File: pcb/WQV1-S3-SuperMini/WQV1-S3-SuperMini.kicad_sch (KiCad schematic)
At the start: 10 parts, among them U1 ESP32-S3 Super Micro, U2 SSD1306_OLED_128x64, U3 TFDU4101-TR3

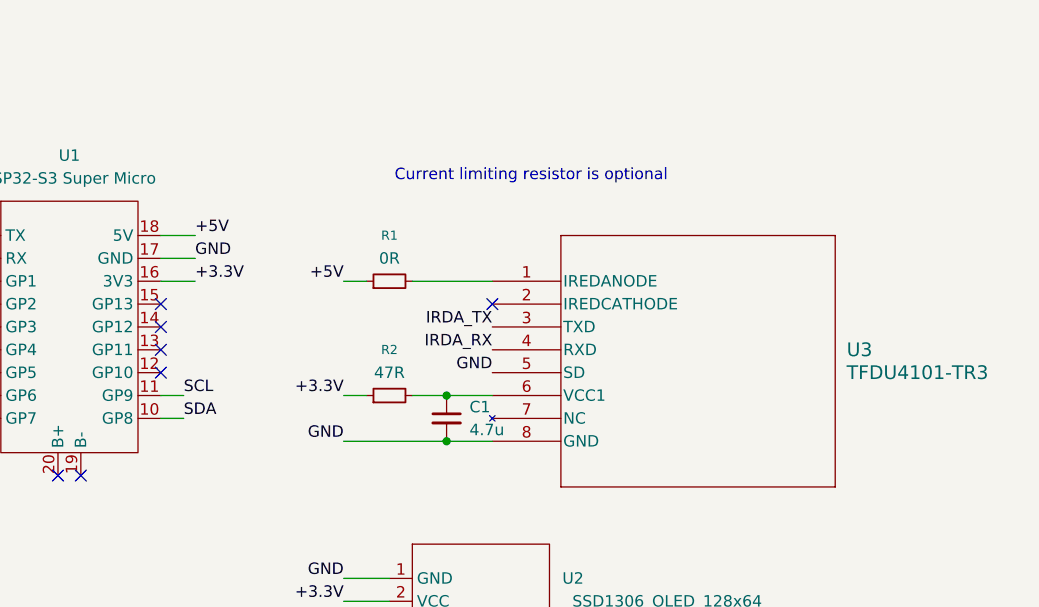
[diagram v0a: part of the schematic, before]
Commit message: PCB revision fixing through-hole spacing
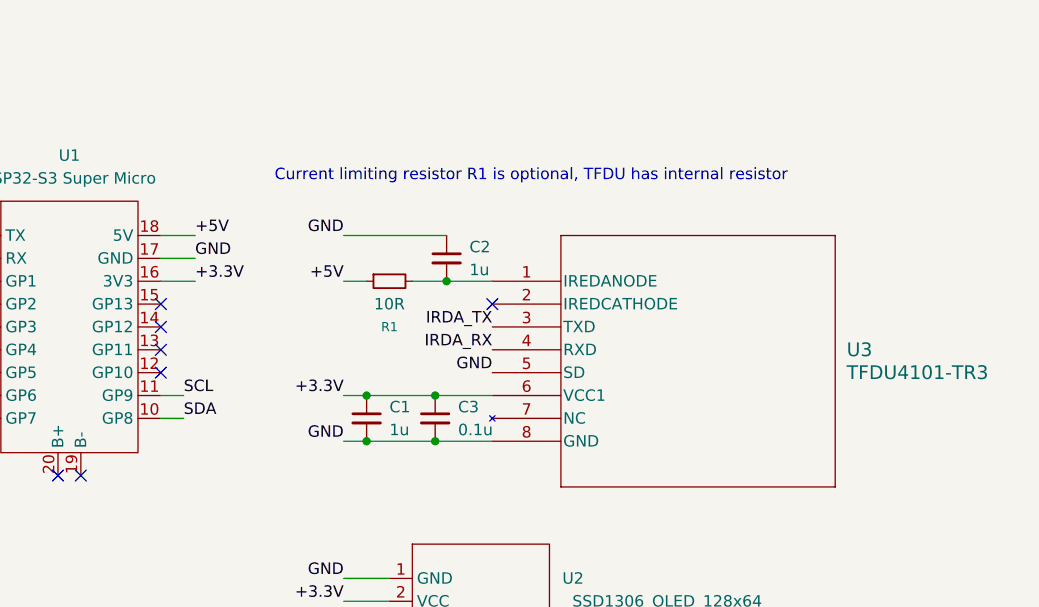
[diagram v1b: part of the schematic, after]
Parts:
- removed R1: 0R, Resistor_SMD:R_0805_2012Metric_Pad1.20x1.40mm_HandSolder, symbol Device:R_Small
- added C2: 1u, Capacitor_SMD:C_0805_2012Metric_Pad1.18x1.45mm_HandSolder, symbol Device:C_Small
- added C3: 0.1u, Capacitor_SMD:C_0805_2012Metric_Pad1.18x1.45mm_HandSolder, symbol Device:C_Small
- C1: value 4.7u -> 1u
- R1: renamed from R2; value 47R -> 10R
- U1: footprint REB_ESP32:ESP32-S3-SuperMicro_SMD -> REB_ESP32:ESP32-S3-SuperMicro_THT
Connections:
- net +3.3V: now also C1.1, U3.6 (VCC1), C3.1; no longer R1.1
- net +5V: now also R1.1
- net GND: now also C2.1, C3.2
- net at U3.1 (IREDANODE): now also R1.2, C2.2
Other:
- note added: "Current limiting resistor R1 is optional, TFDU has internal resistor"
- note removed: "Current limiting resistor is optional"
- company: (none) -> Partlyhuman
- title: (none) -> QV1ckenIR
- moved on the sheet: C1, R1
